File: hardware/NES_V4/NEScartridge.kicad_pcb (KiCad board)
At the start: 4 copper layers, 39 parts, among them J1 Conn_02x36_Top_Bottom, U1 TXS0108EPW, U10 TXS0108EPW, U11 TXS0108EPW, U2 TXS0108EPW, U5 TXS0108EPW, U6 TXS0108EPW, U7 TXS0108EPW, U8 TXS0108EPW, U9 TXS0108EPW

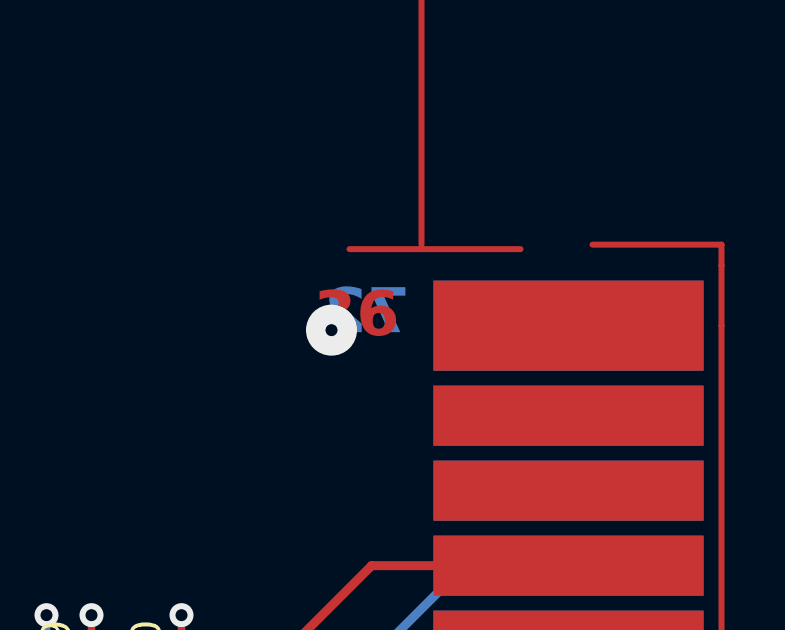
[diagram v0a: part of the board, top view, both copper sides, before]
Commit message: #14 Added GND, 5V and 3.3V layout and fixed some bugs
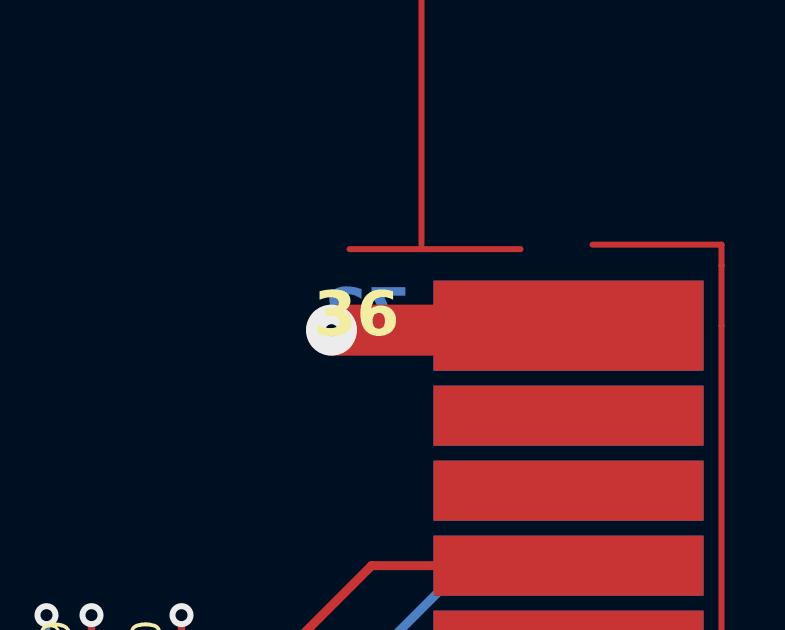
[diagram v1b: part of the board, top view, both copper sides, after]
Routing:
- net +5V: track 148.5 -> 156.5 mm
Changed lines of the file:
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@@
-    (effects (font (size 1.5 1.5) (thickness 0.3) bold) (justify left bottom))
-  )
-  (gr_text "36" (at 151.4 48.35) (layer "F.Cu")
     (effects (font (size 1.5 1.5) (thickness 0.3) bold) (justify left bottom))
   )
@@
   (gr_text "72\n" (at 154.6 48.25) (layer "B.Cu")
     (effects (font (size 1.5 1.5) (thickness 0.3) bold) (justify left bottom mirror))
+  )
+  (gr_text "36" (at 151.4 48.35) (layer "F.SilkS")
+    (effects (font (size 1.5 1.5) (thickness 0.3) bold) (justify left bottom))
   )
   (segment (start 142.5 130) (end 142.5 129.0975) (width 0.25) (layer "F.Cu") (net 1))
@@
   (segment (start 147.525 61.575) (end 147 61.05) (width 0.3) (layer "F.Cu") (net 105))
   (segment (start 144.5 101.798898) (end 145.401102 102.7) (width 0.3) (layer "F.Cu") (net 105))
+  (segment (start 152 48) (end 159.75 48) (width 1.7) (layer "F.Cu") (net 105))
   (segment (start 144.5 100.48) (end 144.5 101.798898) (width 0.3) (layer "F.Cu") (net 105))
   (segment (start 148.2625 74.075) (end 147.525 74.075) (width 0.3) (layer "F.Cu") (net 105))
@@
   (segment (start 156.4 47.85) (end 159.4 47.85) (width 0.3) (layer "F.Cu") (net 105))
   (segment (start 148.2625 61.575) (end 147.525 61.575) (width 0.3) (layer "F.Cu") (net 105))
+  (segment (start 159.75 48) (end 159.9 47.85) (width 1.7) (layer "F.Cu") (net 105))
   (segment (start 145.401102 102.7) (end 145.65 102.7) (width 0.3) (layer "F.Cu") (net 105))
   (segment (start 147.525 74.075) (end 147 73.55) (width 0.3) (layer "F.Cu") (net 105))
@@
         (xy 155 138)
         (xy 86.5 138)
-        (xy 86.5 138)
-        (xy 86.5 45.5)
         (xy 86.5 45.5)
       )
